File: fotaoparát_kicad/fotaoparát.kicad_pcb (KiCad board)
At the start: 4 copper layers, 6 parts, among them IC1 W25Q256JVEIQ, J1 Conn_01x22, J2 Micro_SD_Card_Det1

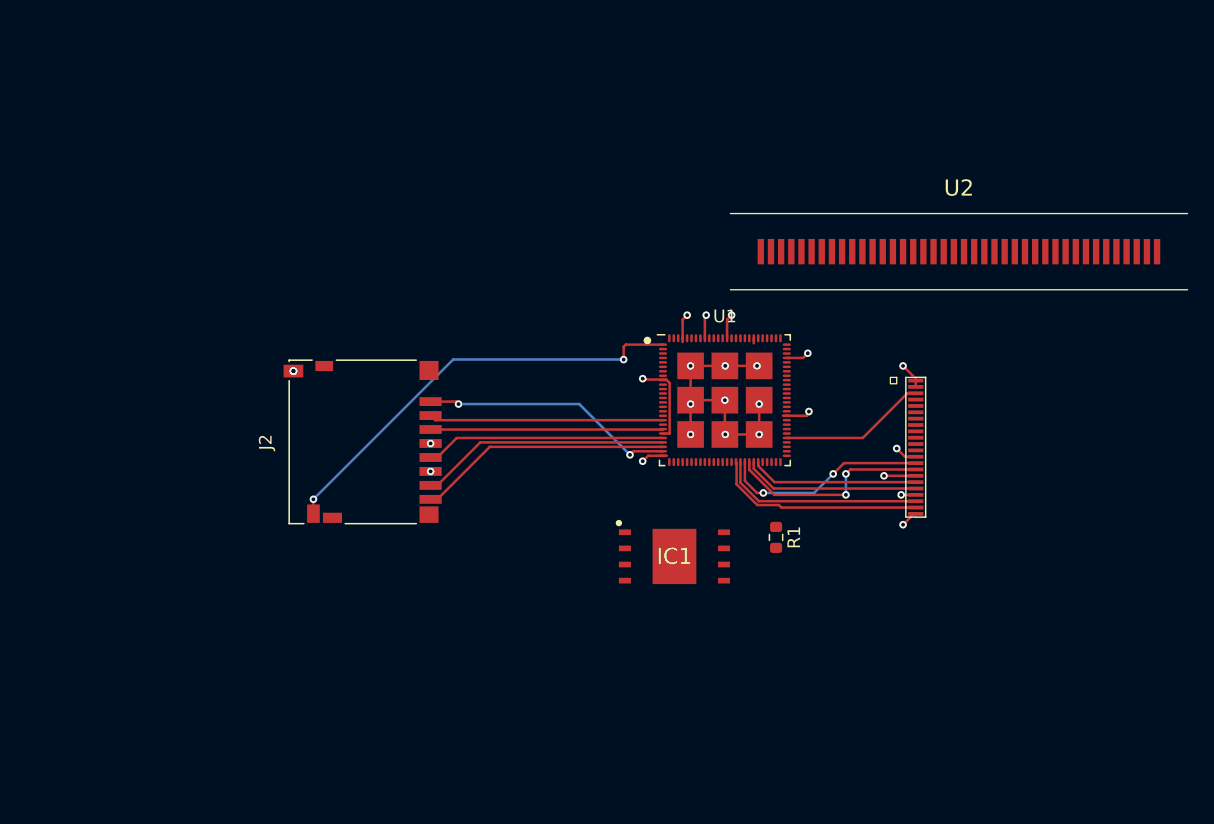
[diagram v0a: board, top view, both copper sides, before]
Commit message: Uprava pcb, finalni predelani (snad)  kamery
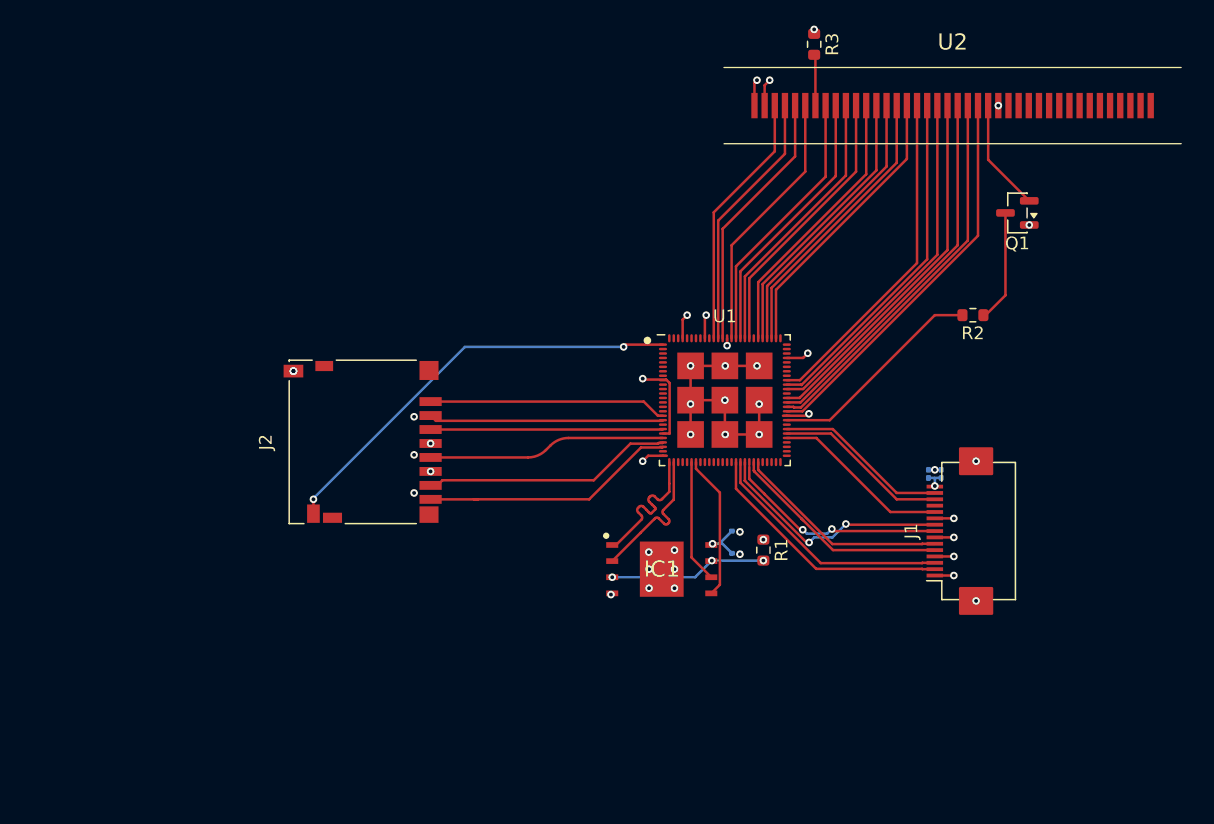
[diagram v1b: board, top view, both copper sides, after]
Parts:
- added C1: 100nF, Capacitor_SMD:C_0201_0603Metric, B.Cu at (157.3, 95.8)
- added C2: 1uF, Capacitor_SMD:C_0201_0603Metric, B.Cu at (157.3, 94.0)
- added C3: 4,7uF, Capacitor_SMD:C_0201_0603Metric, B.Cu at (173.5, 89.5)
- added C4: 100nF, Capacitor_SMD:C_0201_0603Metric, B.Cu at (172.5, 89.5)
- added Q1: AO3400A, Package_TO_SOT_SMD:SOT-23, F.Cu at (179.5, 69.0)
- added R2: 100R, Resistor_SMD:R_0603_1608Metric, F.Cu at (176.0, 77.0)
- added R3: 10k, Resistor_SMD:R_0603_1608Metric, F.Cu at (163.5, 55.7)
- J1: value Conn_01x22 -> Conn_01x15_Pin; footprint rnd_shit_co_nema_symboly:Hirose_FH12-22S-0.5SH -> Connector_FFC-FPC:Hirose_FH12-15S-0.5SH_1x15-1MP_P0.50mm_Horizontal
- moved U2 11.5 mm to (174.4, 60.5)
- moved J1 7.83 mm to (174.8, 94.0), turned to 90 degrees
- moved IC1 1.41 mm to (151.5, 97.0)
- moved R1 1.41 mm to (159.5, 95.5)
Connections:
- J1 pad 1: +3.3V -> GND
- J1 pad 10: unconnected-(J1-Pin_10-Pad10) -> GND
- J1 pad 11: unconnected-(J1-Pin_11-Pad11) -> Net-(J1-Pin_11)
- J1 pad 13: GND -> Net-(J1-Pin_13)
- J1 pad 15: Net-(J1-Pin_15) -> +3.3V
- J1 pad 2: +3.3V -> /CSI_DATA_N0
- J1 pad 3: Net-(J1-Pin_3) -> /CSI_DATA_P0
- J1 pad 4: Net-(J1-Pin_4) -> GND
- J1 pad 5: unconnected-(J1-Pin_5-Pad5) -> /CSI_DATA_N1
- J1 pad 6: Net-(J1-Pin_6) -> /CSI_DATA_P1
- J1 pad 7: unconnected-(J1-Pin_7-Pad7) -> GND
- J1 pad 8: unconnected-(J1-Pin_8-Pad8) -> /CSI_CLK_N
- J1 pad 9: unconnected-(J1-Pin_9-Pad9) -> /CSI_CLK_P
- U1 pad 17: unconnected-(U1-GPIO16/ADC-Pad17) -> Net-(J2-DAT2)
- U1 pad 25: Net-(J2-DAT2) -> unconnected-(U1-GPIO23/ADC-Pad25)
- U1 pad 42: Net-(J1-Pin_21) -> /CSI_DATA_N0
- U1 pad 43: Net-(J1-Pin_20) -> /CSI_DATA_P0
- U1 pad 44: Net-(J1-Pin_14) -> /CSI_CLK_P
- U1 pad 45: Net-(J1-Pin_15) -> /CSI_CLK_N
- U1 pad 46: Net-(J1-Pin_18) -> /CSI_DATA_N1
- U1 pad 47: Net-(J1-Pin_17) -> /CSI_DATA_P1
- U1 pad 57: Net-(J1-Pin_3) -> Net-(J1-Pin_11)
- U1 pad 58: Net-(J1-Pin_4) -> Net-(J1-Pin_13)
- U1 pad 59: unconnected-(U1-VDD_PSRAM_0-Pad59) -> Net-(J1-Pin_14)
- U1 pad 60: Net-(J1-Pin_6) -> unconnected-(U1-GPIO30-Pad60)
- U1 pad 61: unconnected-(U1-GPIO31-Pad61) -> Net-(U1-GPIO31)
- U1 pad 63: unconnected-(U1-GPIO32-Pad63) -> Net-(U1-GPIO32)
- U1 pad 64: unconnected-(U1-GPIO33-Pad64) -> Net-(U1-GPIO33)
- U1 pad 65: unconnected-(U1-GPIO34-Pad65) -> Net-(U1-GPIO34)
- U1 pad 66: unconnected-(U1-GPIO35-Pad66) -> Net-(U1-GPIO35)
- U1 pad 68: unconnected-(U1-GPIO36-Pad68) -> Net-(U1-GPIO36)
- U1 pad 69: unconnected-(U1-GPIO37-Pad69) -> Net-(U1-GPIO37)
- U1 pad 70: unconnected-(U1-GPIO38-Pad70) -> Net-(U1-GPIO38)
- U1 pad 80: unconnected-(U1-GPIO39-Pad80) -> Net-(U1-GPIO39)
- U1 pad 81: unconnected-(U1-GPIO40-Pad81) -> Net-(U1-GPIO40)
- U1 pad 82: unconnected-(U1-GPIO41-Pad82) -> Net-(U1-GPIO41)
- U1 pad 83: unconnected-(U1-GPIO42-Pad83) -> Net-(U1-GPIO42)
- U1 pad 84: unconnected-(U1-GPIO43-Pad84) -> Net-(U1-GPIO43)
- U1 pad 86: unconnected-(U1-GPIO44-Pad86) -> Net-(U1-GPIO44)
- U1 pad 87: unconnected-(U1-GPIO45-Pad87) -> Net-(U1-GPIO45)
- U1 pad 88: unconnected-(U1-GPIO46-Pad88) -> Net-(U1-GPIO46)
- U1 pad 89: unconnected-(U1-GPIO47-Pad89) -> Net-(U1-GPIO47)
- U1 pad 90: unconnected-(U1-GPIO48-Pad90) -> Net-(U1-GPIO48)
- U1 pad 92: unconnected-(U1-GPIO49/ADC-Pad92) -> Net-(U1-GPIO49/ADC)
- U1 pad 93: unconnected-(U1-GPIO50/ADC-Pad93) -> Net-(U1-GPIO50/ADC)
- U1 pad 94: unconnected-(U1-GPIO51/ADC-Pad94) -> Net-(U1-GPIO51/ADC)
- U2 pad 10: unconnected-(U2-D2-Pad10) -> Net-(U1-GPIO45)
- U2 pad 11: unconnected-(U2-D3-Pad11) -> Net-(U1-GPIO44)
- U2 pad 12: unconnected-(U2-D4-Pad12) -> Net-(U1-GPIO43)
- U2 pad 13: unconnected-(U2-D5-Pad13) -> Net-(U1-GPIO42)
- U2 pad 14: unconnected-(U2-D6-Pad14) -> Net-(U1-GPIO41)
- U2 pad 15: unconnected-(U2-D7-Pad15) -> Net-(U1-GPIO40)
- U2 pad 16: unconnected-(U2-D8-Pad16) -> Net-(U1-GPIO39)
- U2 pad 17: unconnected-(U2-D9-Pad17) -> Net-(U1-GPIO38)
- U2 pad 18: unconnected-(U2-D10-Pad18) -> Net-(U1-GPIO37)
- U2 pad 19: unconnected-(U2-D11-Pad19) -> Net-(U1-GPIO36)
- U2 pad 20: unconnected-(U2-D12-Pad20) -> Net-(U1-GPIO35)
- U2 pad 21: unconnected-(U2-D13-Pad21) -> Net-(U1-GPIO34)
- U2 pad 22: unconnected-(U2-D14-Pad22) -> Net-(U1-GPIO33)
- U2 pad 23: unconnected-(U2-D15-Pad23) -> Net-(U1-GPIO32)
- U2 pad 24: unconnected-(U2-LEDK-Pad24) -> Net-(Q1-S)
- U2 pad 25: unconnected-(U2-LEDA-Pad25) -> +3.3V
- U2 pad 3: unconnected-(U2-RESET-Pad3) -> Net-(U1-GPIO51/ADC)
- U2 pad 4: unconnected-(U2-CS-Pad4) -> Net-(U1-GPIO50/ADC)
- U2 pad 5: unconnected-(U2-RS/DC-Pad5) -> Net-(U1-GPIO49/ADC)
- U2 pad 6: unconnected-(U2-WR-Pad6) -> Net-(U1-GPIO48)
- U2 pad 7: +3.3V -> Net-(U2-RD)
- U2 pad 8: unconnected-(U2-D0-Pad8) -> Net-(U1-GPIO47)
- U2 pad 9: unconnected-(U2-D1-Pad9) -> Net-(U1-GPIO46)
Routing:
- net Net-(U1-GPIO32): track 0.00 -> 31.0 mm
- net Net-(U1-GPIO33): track 0.00 -> 30.3 mm
- net Net-(U1-GPIO34): track 0.00 -> 29.6 mm
- net Net-(U1-GPIO35): track 0.00 -> 28.9 mm
- net Net-(U1-GPIO36): track 0.00 -> 28.0 mm
- net Net-(U1-GPIO37): track 0.00 -> 27.3 mm
- net Net-(U1-GPIO38): track 0.00 -> 26.5 mm
- net Net-(U1-GPIO39): track 0.00 -> 22.6 mm
- net Net-(U1-GPIO40): track 0.00 -> 22.4 mm
- net Net-(U1-GPIO41): track 0.00 -> 22.2 mm
- net Net-(U1-GPIO42): track 0.00 -> 22.0 mm
- net Net-(U1-GPIO43): track 0.00 -> 21.8 mm
- net Net-(U1-GPIO44): track 0.00 -> 21.8 mm
- net Net-(U1-GPIO45): track 0.00 -> 21.6 mm
- net Net-(U1-GPIO46): track 0.00 -> 21.4 mm
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- added copper zone on In2.Cu, net +3.3V
- added copper zone on In1.Cu, net GND
- removed copper zone on In1.Cu, net +3.3V
- removed copper zone on In2.Cu, net GND

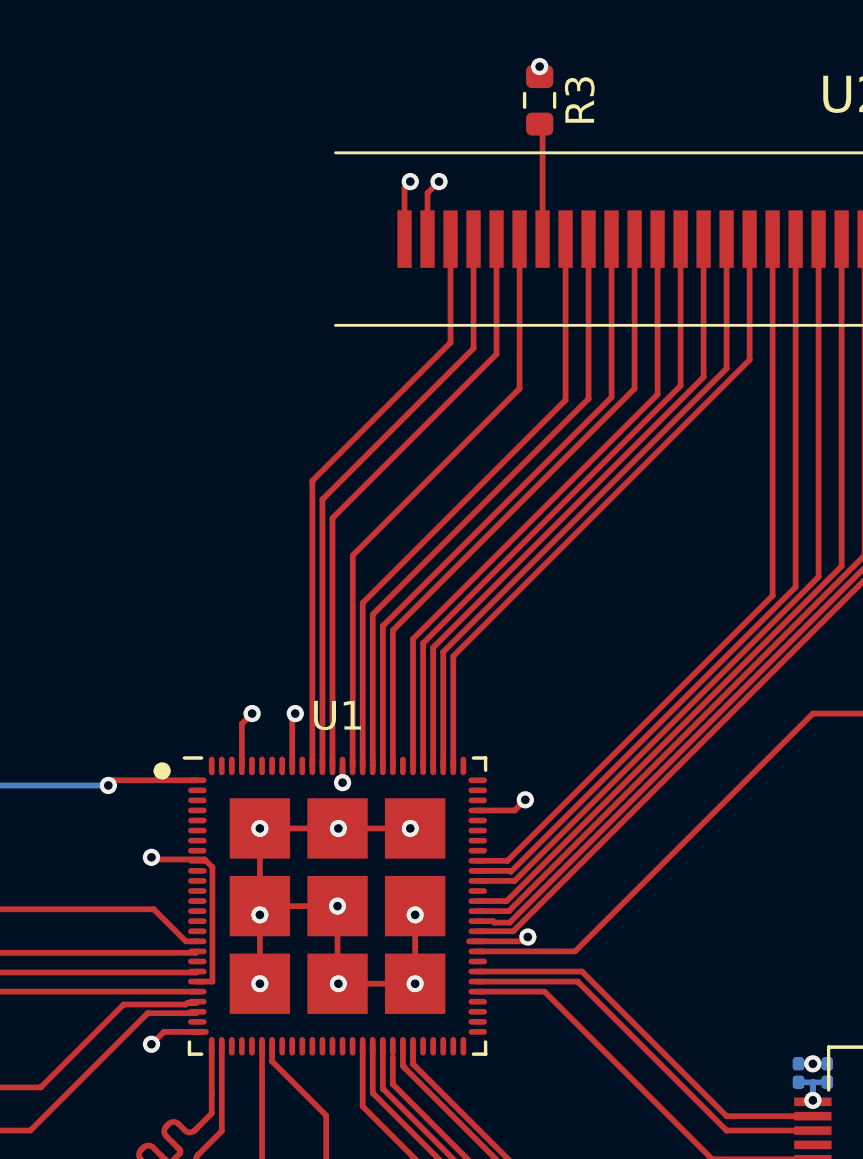
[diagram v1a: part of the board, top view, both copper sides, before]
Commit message: Zvyseni prehlednosti schametu
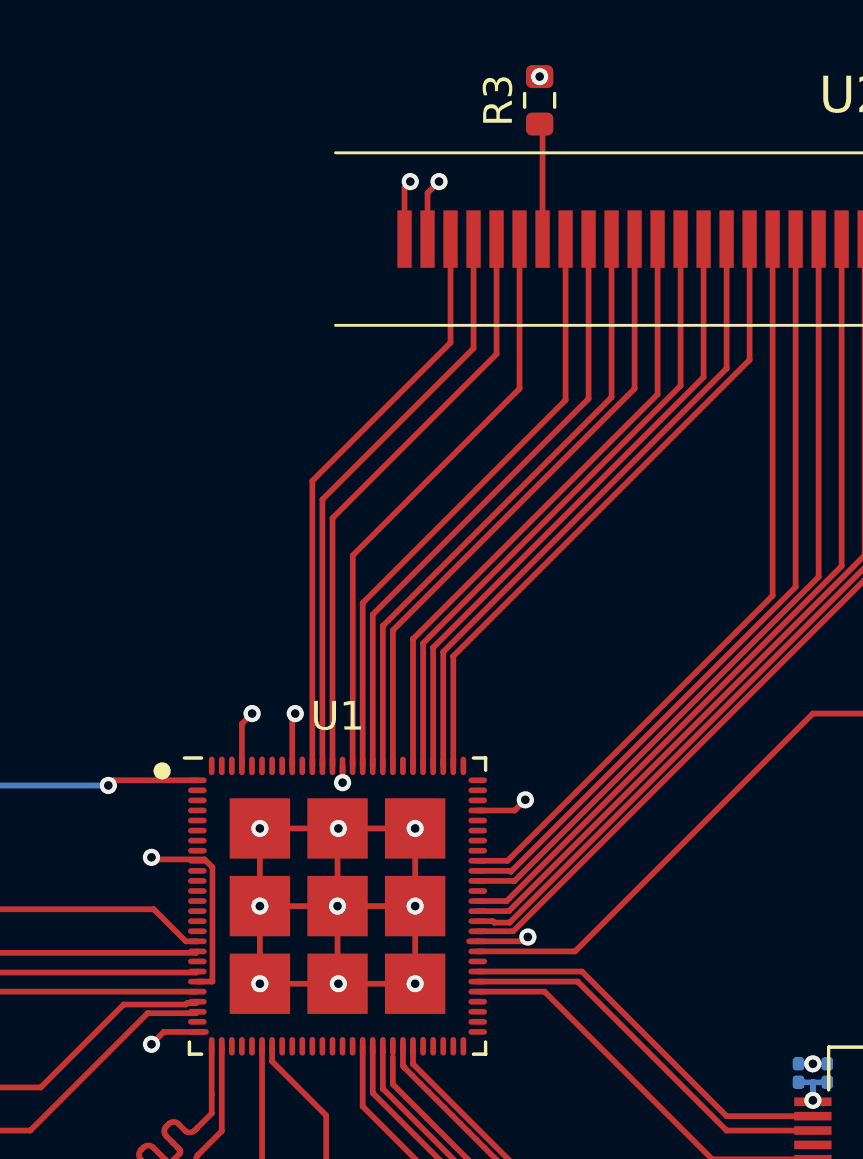
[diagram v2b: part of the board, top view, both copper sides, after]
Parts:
- turned R3 to 90 degrees
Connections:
- net Net-(Q1-S) renamed /LEDK
- net Net-(U1-GPIO32) renamed /D15
- net Net-(U1-GPIO33) renamed /D14
- net Net-(U1-GPIO34) renamed /D13
- net Net-(U1-GPIO35) renamed /D12
- net Net-(U1-GPIO36) renamed /D11
- net Net-(U1-GPIO37) renamed /D10
- net Net-(U1-GPIO38) renamed /D9
- net Net-(U1-GPIO39) renamed /D8
- net Net-(U1-GPIO40) renamed /D7
- net Net-(U1-GPIO41) renamed /D6
- net Net-(U1-GPIO42) renamed /D5
- net Net-(U1-GPIO43) renamed /D4
- net Net-(U1-GPIO44) renamed /D3
- net Net-(U1-GPIO45) renamed /D2
- net Net-(U1-GPIO46) renamed /D1
- net Net-(U1-GPIO47) renamed /D0
- net Net-(U1-GPIO48) renamed /WR
- net Net-(U1-GPIO49/ADC) renamed /RS/DC
- net Net-(U1-GPIO50/ADC) renamed /CS
- net Net-(U1-GPIO51/ADC) renamed /RESET
- J1 pad MP: GND -> (no net)
- R3 pad 1: +3.3V -> Net-(U2-RD)
- R3 pad 2: Net-(U2-RD) -> +3.3V
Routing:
- net GND: track 31.3 -> 42.1 mm

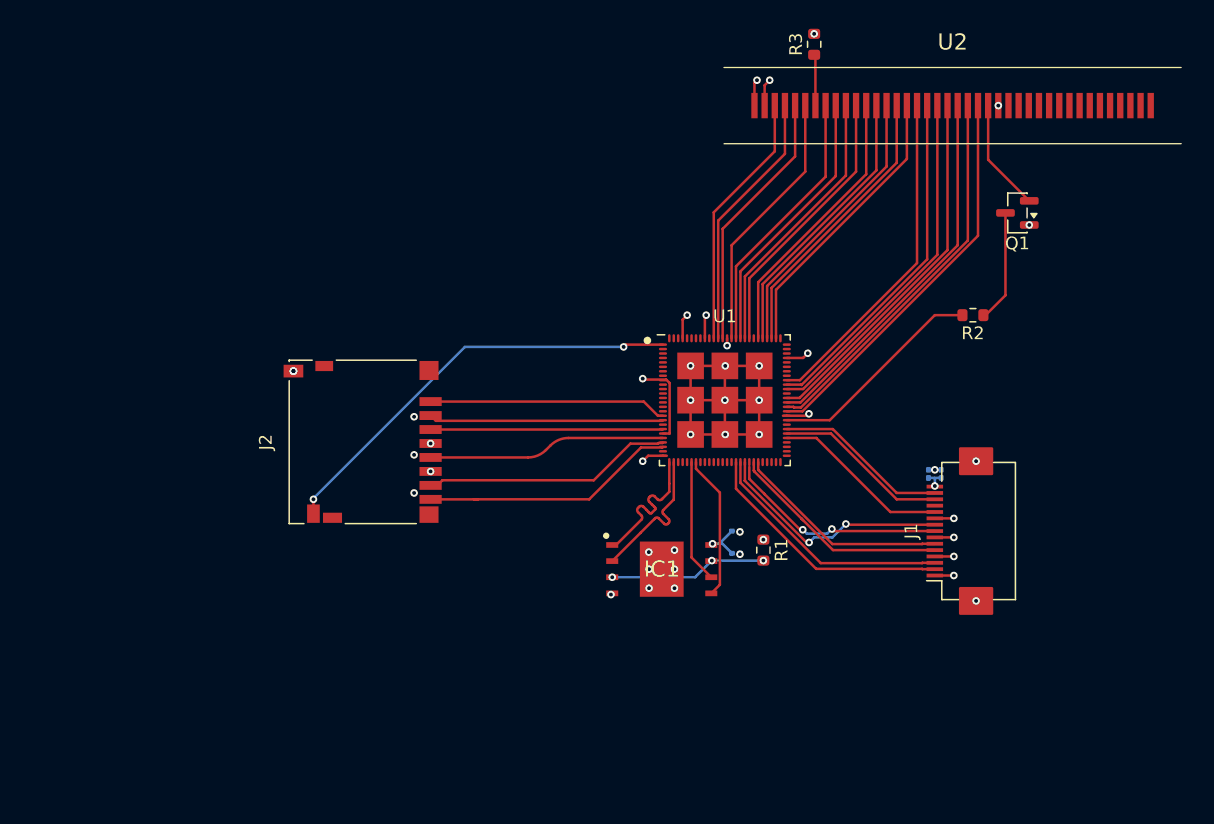
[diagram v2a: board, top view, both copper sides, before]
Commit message: Udelal jsem znovu sd kartovy dock, tentokrat je spravne orientovany to same s konktorem na display
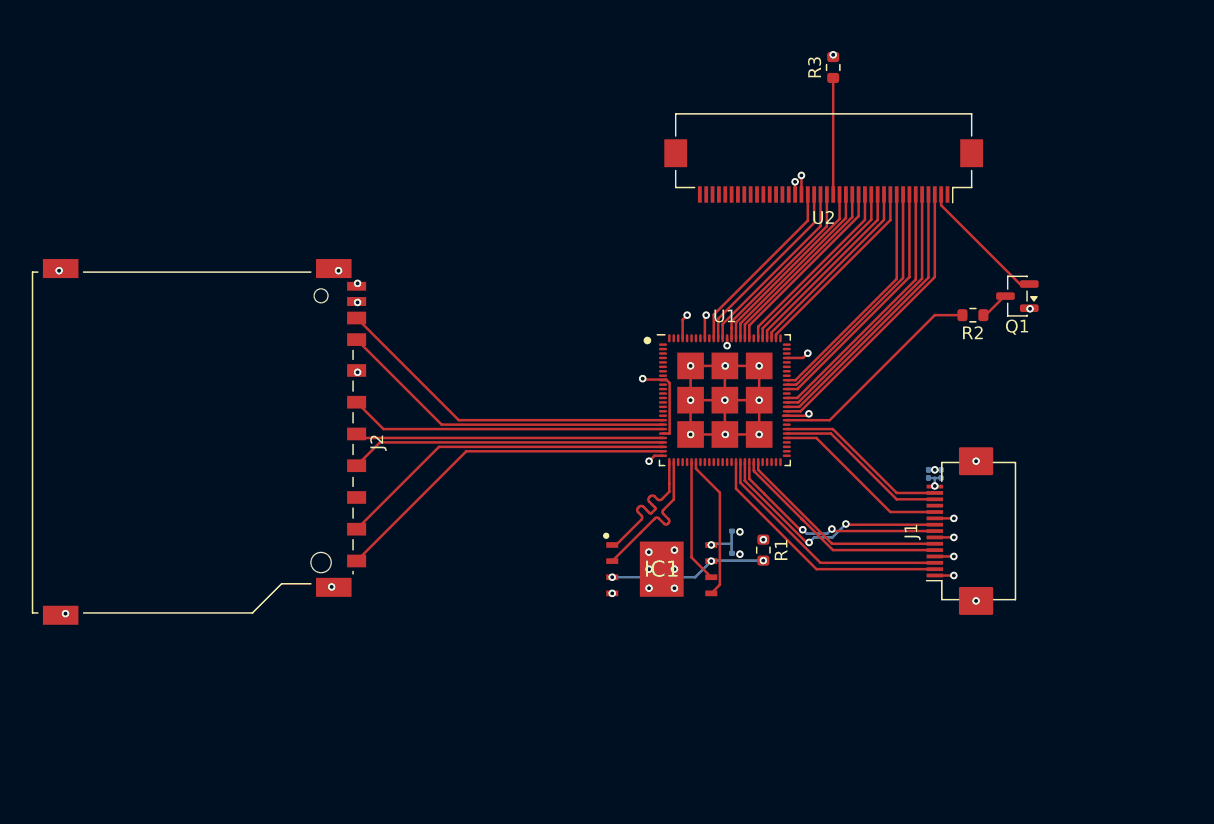
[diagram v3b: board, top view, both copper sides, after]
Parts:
- J2: footprint Connector_Card:microSD_HC_Hirose_DM3D-SF -> Connector_Card:SD_TE_2041021
- U2: footprint stlib:ST7796s_40PIN_0.8MM -> Connector_FFC-FPC:Hirose_FH12-40S-0.5SH_1x40-1MP_P0.50mm_Horizontal
- moved J2 12.5 mm to (115.5, 87.0), turned to -90 degrees
- moved U2 11.4 mm to (164.2, 65.7), turned to 180 degrees
- moved Q1 6.55 mm to (179.5, 75.5)
- moved R3 2.36 mm to (165.0, 57.5)
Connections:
- J2 pad 1: Net-(J2-DAT2) -> /dat2
- J2 pad 2: Net-(J2-DAT3/CD) -> /dat3/cd
- J2 pad 3: Net-(J2-CMD) -> /cmd
- J2 pad 4: +3.3V -> /vdd
- J2 pad 5: Net-(J2-CLK) -> /clk
- J2 pad 7: Net-(J2-DAT0) -> /dat0
- J2 pad 8: Net-(J2-DAT1) -> /dat1
- J2 pad 9: Net-(J2-DET) -> /det
- R3 pad 1: Net-(U2-RD) -> Net-(U2-pin19)
- U1 pad 1: Net-(J2-DET) -> unconnected-(U1-GPIO1/ADC-Pad1)
- U1 pad 17: Net-(J2-DAT2) -> unconnected-(U1-GPIO16/ADC-Pad17)
- U1 pad 18: Net-(J2-DAT3/CD) -> /dat1
- U1 pad 19: unconnected-(U1-GPIO18/ADC-Pad19) -> /dat0
- U1 pad 20: Net-(J2-CMD) -> /clk
- U1 pad 22: Net-(J2-CLK) -> /vdd
- U1 pad 23: Net-(J2-DAT0) -> /cmd
- U1 pad 24: Net-(J2-DAT1) -> /dat2
- U1 pad 25: unconnected-(U1-GPIO23/ADC-Pad25) -> /det
- U2 pad 10: /D2 -> /D8
- U2 pad 11: /D3 -> /D7
- U2 pad 12: /D4 -> /D6
- U2 pad 14: /D6 -> /D4
- U2 pad 15: /D7 -> /D3
- U2 pad 16: /D8 -> /D2
- U2 pad 17: /D9 -> /D1
- U2 pad 18: /D10 -> /D0
- U2 pad 19: /D11 -> Net-(U2-pin19)
- U2 pad 2: GND -> /LEDK
- U2 pad 20: /D12 -> /WR
- U2 pad 21: /D13 -> /RS/DC
- U2 pad 22: /D14 -> /CS
- U2 pad 23: /D15 -> /RESET
- U2 pad 24: /LEDK -> GND
- U2 pad 3: /RESET -> /D15
- U2 pad 4: /CS -> /D14
- U2 pad 5: /RS/DC -> /D13
- U2 pad 6: /WR -> /D12
- U2 pad 7: Net-(U2-RD) -> /D11
- U2 pad 8: /D0 -> /D10
- U2 pad 9: /D1 -> /D9
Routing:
- net Net-(J2-DET): track 33.7 -> 0.00 mm, vias 2 -> 0
- net /det: track 0.00 -> 27.7 mm
- net /dat1: track 0.00 -> 27.5 mm
- net /dat0: track 0.00 -> 26.9 mm
- net /dat2: track 0.00 -> 26.8 mm
- net /clk: track 0.00 -> 25.0 mm
- net /cmd: track 0.00 -> 24.9 mm
- net /vdd: track 0.00 -> 24.3 mm
- net Net-(J2-DAT1): track 20.3 -> 0.00 mm
- net Net-(J2-DAT0): track 19.7 -> 0.00 mm
- net Net-(J2-DAT2): track 18.8 -> 0.00 mm
- net Net-(J2-CLK): track 18.7 -> 0.00 mm
- net Net-(J2-DAT3/CD): track 18.5 -> 0.00 mm
- net Net-(J2-CMD): track 18.3 -> 0.00 mm
- net Net-(U2-pin19): track 0.00 -> 9.17 mm
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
